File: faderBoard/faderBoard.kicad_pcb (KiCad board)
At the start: 2 copper layers, 80 x 80 mm, 22 parts, among them J1 Conn_01x14_Pin, J2 Conn_01x14_Socket, U1 ADS1115IDGS

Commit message: placed pinHeaders
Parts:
- J1, J2: moved to B.Cu
- moved J2 123.3 mm to (69.8, 23.4), turned to 180 degrees
- moved J1 65.5 mm to (4.00, 23.5), turned to 180 degrees
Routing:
- net in2: track 0.00 -> 70.0 mm
- net in1: track 0.00 -> 70.0 mm
- net Net-(J1-Pin_9): track 0.00 -> 70.0 mm
- net Net-(J1-Pin_14): track 0.00 -> 70.0 mm
- net Net-(J1-Pin_13): track 0.00 -> 70.0 mm
- net Net-(J1-Pin_12): track 0.00 -> 70.0 mm
- net Net-(J1-Pin_11): track 0.00 -> 70.0 mm
- net Net-(J1-Pin_10): track 0.00 -> 70.0 mm

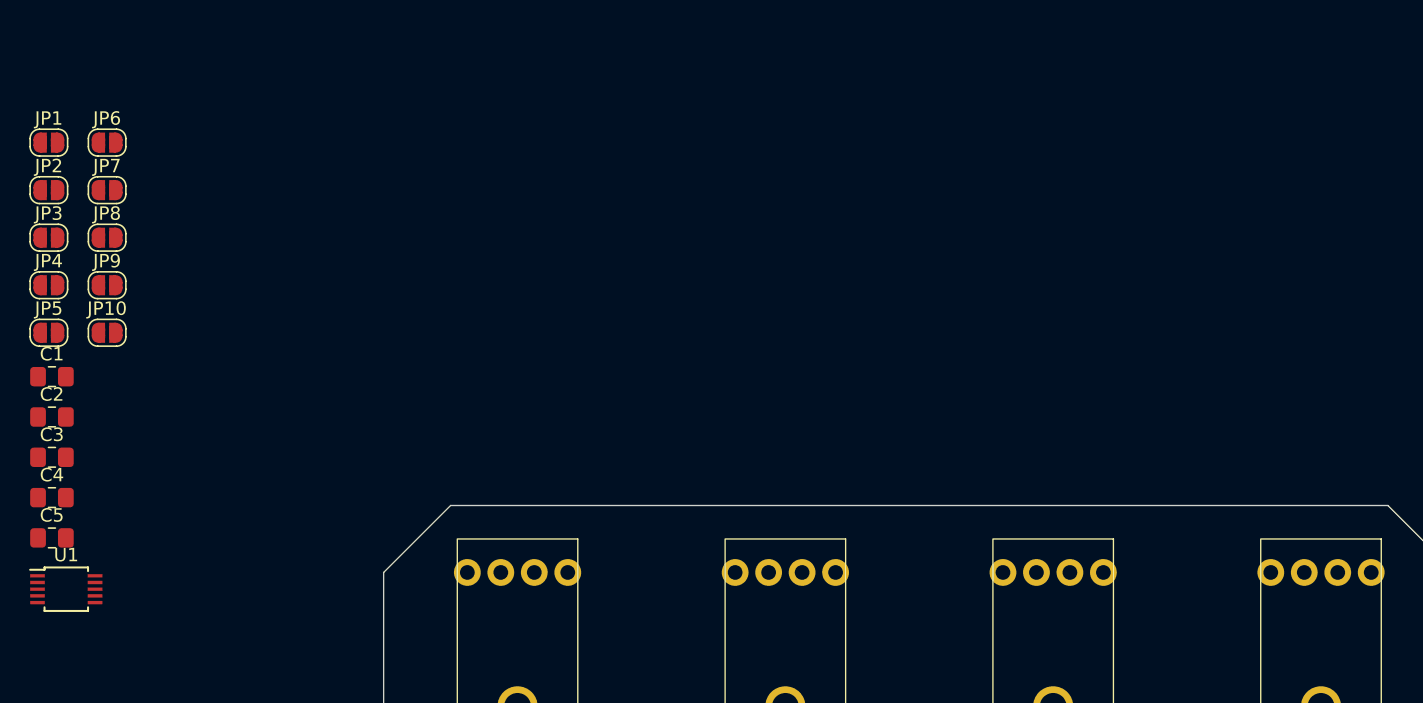
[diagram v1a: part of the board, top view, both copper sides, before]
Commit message: placed fader caps
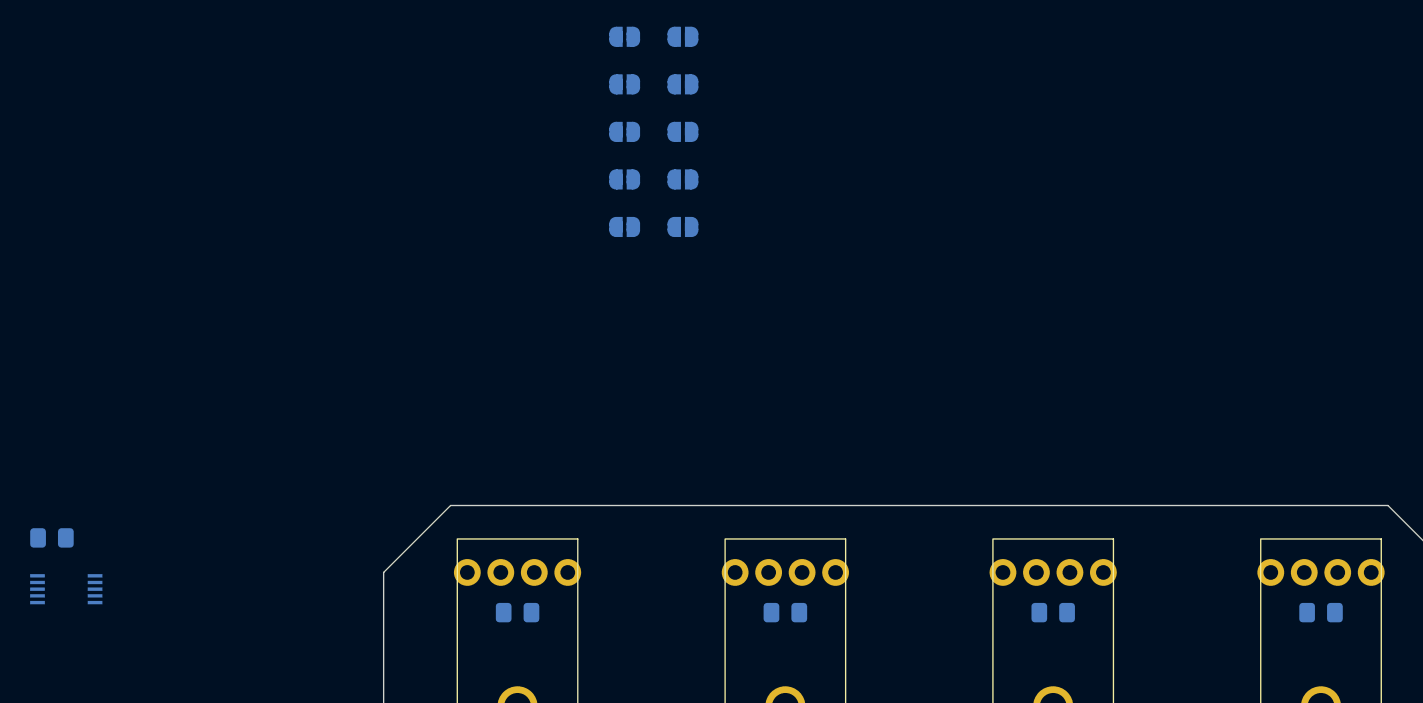
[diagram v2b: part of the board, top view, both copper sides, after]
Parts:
- C1, C2, C3, C4, C5, JP1, JP10, JP2, JP3, JP4, JP5, JP6, JP7, JP8, JP9, U1: moved to B.Cu
- moved C4 95.2 mm to (70.0, 8.00)
- moved C3 75.7 mm to (50.0, 8.00)
- moved C2 56.7 mm to (30.0, 8.00)
- moved JP1 43.7 mm to (18.0, -35.0), turned to 180 degrees
- moved JP10 43.7 mm to (22.4, -20.8), turned to 180 degrees
- moved JP2 43.7 mm to (18.0, -31.4), turned to 180 degrees
- moved JP3 43.7 mm to (18.0, -27.9), turned to 180 degrees
- moved JP4 43.7 mm to (18.0, -24.4), turned to 180 degrees
- moved JP5 43.7 mm to (18.0, -20.8), turned to 180 degrees
- moved JP6 43.7 mm to (22.4, -35.0), turned to 180 degrees
- moved JP7 43.7 mm to (22.4, -31.4), turned to 180 degrees
- moved JP8 43.7 mm to (22.4, -27.9), turned to 180 degrees
- moved JP9 43.7 mm to (22.4, -24.4), turned to 180 degrees
- moved C1 39.0 mm to (10.0, 8.00), turned to 180 degrees
- turned C5 to 180 degrees
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
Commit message: placed adc
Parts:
- moved C5 65.4 mm to (40.0, 12.0)
- moved U1 64.3 mm to (40.0, 15.0), turned to 0 degrees
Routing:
- net Fader4: track 0.00 -> 35.7 mm
- net Fader1: track 0.00 -> 28.0 mm
- net Fader3: track 0.00 -> 15.5 mm
- net Fader2: track 0.00 -> 13.4 mm
- net VCC: track 0.00 -> 3.96 mm
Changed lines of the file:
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@@
   )
   (footprint "Package_SO:TSSOP-10_3x3mm_P0.5mm" (layer "B.Cu")
-    (at -23.7 6.25 180)
+    (at 40 15)
     (descr "TSSOP10: plastic thin shrink small outline package; 10 leads; body width 3 mm; (see NXP SSOP-TSSOP-VSO-REFLOW.pdf and sot552-1_po.pdf)")
     (tags "SSOP 0.5")
@@
     (fp_line (start 1.5 1.5) (end 1.5 -1.5)
       (stroke (width 0.1) (type solid)) (layer "B.Fab"))
-    (pad "1" smd rect (at -2.15 1 180) (size 1.1 0.25) (layers "B.Cu" "B.Paste" "B.Mask")
+    (pad "1" smd rect (at -2.15 1) (size 1.1 0.25) (layers "B.Cu" "B.Paste" "B.Mask")
       (net 22 "ADDR") (pinfunction "ADDR") (pintype "input"))
-    (pad "2" smd rect (at -2.15 0.5 180) (size 1.1 0.25) (layers "B.Cu" "B.Paste" "B.Mask")
+    (pad "2" smd rect (at -2.15 0.5) (size 1.1 0.25) (layers "B.Cu" "B.Paste" "B.Mask")
       (net 35 "ALERT") (pinfunction "ALERT/RDY") (pintype "output"))
-    (pad "3" smd rect (at -2.15 0 180) (size 1.1 0.25) (layers "B.Cu" "B.Paste" "B.Mask")
+    (pad "3" smd rect (at -2.15 0) (size 1.1 0.25) (layers "B.Cu" "B.Paste" "B.Mask")
       (net 1 "GND") (pinfunction "GND") (pintype "power_in"))
-    (pad "4" smd rect (at -2.15 -0.5 180) (size 1.1 0.25) (layers "B.Cu" "B.Paste" "B.Mask")
+    (pad "4" smd rect (at -2.15 -0.5) (size 1.1 0.25) (layers "B.Cu" "B.Paste" "B.Mask")
       (net 2 "Fader1") (pinfunction "AIN0") (pintype "input"))
-    (pad "5" smd rect (at -2.15 -1 180) (size 1.1 0.25) (layers "B.Cu" "B.Paste" "B.Mask")
+    (pad "5" smd rect (at -2.15 -1) (size 1.1 0.25) (layers "B.Cu" "B.Paste" "B.Mask")
       (net 3 "Fader2") (pinfunction "AIN1") (pintype "input"))
-    (pad "6" smd rect (at 2.15 -1 180) (size 1.1 0.25) (layers "B.Cu" "B.Paste" "B.Mask")
+    (pad "6" smd rect (at 2.15 -1) (size 1.1 0.25) (layers "B.Cu" "B.Paste" "B.Mask")
       (net 4 "Fader3") (pinfunction "AIN2") (pintype "input"))
-    (pad "7" smd rect (at 2.15 -0.5 180) (size 1.1 0.25) (layers "B.Cu" "B.Paste" "B.Mask")
+    (pad "7" smd rect (at 2.15 -0.5) (size 1.1 0.25) (layers "B.Cu" "B.Paste" "B.Mask")
       (net 5 "Fader4") (pinfunction "AIN3") (pintype "input"))
-    (pad "8" smd rect (at 2.15 0 180) (size 1.1 0.25) (layers "B.Cu" "B.Paste" "B.Mask")
+    (pad "8" smd rect (at 2.15 0) (size 1.1 0.25) (layers "B.Cu" "B.Paste" "B.Mask")
       (net 6 "VCC") (pinfunction "VDD") (pintype "power_in"))
-    (pad "9" smd rect (at 2.15 0.5 180) (size 1.1 0.25) (layers "B.Cu" "B.Paste" "B.Mask")
+    (pad "9" smd rect (at 2.15 0.5) (size 1.1 0.25) (layers "B.Cu" "B.Paste" "B.Mask")
       (net 7 "SDA") (pinfunction "SDA") (pintype "bidirectional"))
-    (pad "10" smd rect (at 2.15 1 180) (size 1.1 0.25) (layers "B.Cu" "B.Paste" "B.Mask")
+    (pad "10" smd rect (at 2.15 1) (size 1.1 0.25) (layers "B.Cu" "B.Paste" "B.Mask")
       (net 8 "SCL") (pinfunction "SCL") (pintype "input"))
     (model "${KICAD6_3DMODEL_DIR}/Package_SO.3dshapes/TSSOP-10_3x3mm_P0.5mm.wrl"
@@
   )
   (footprint "Capacitor_SMD:C_0805_2012Metric_Pad1.18x1.45mm_HandSolder" (layer "B.Cu")
-    (at -24.77 2.42 180)
+    (at 39.9625 12 180)
     (descr "Capacitor SMD 0805 (2012 Metric), square (rectangular) end terminal, IPC_7351 nominal with elongated pad for handsoldering. (Body size source: IPC-SM-782 page 76, https://www.pcb-3d.com/wordpress/wp-content/uploads/ipc-sm-782a_amendment_1_and_2.pdf, https://docs.google.com/spreadsheets/d/1BsfQQcO9C6DZCsRaXUlFlo91Tg2WpOkGARC1WS5S8t0/edit?usp=sharing), generated with kicad-footprint-generator")
     (tags "capacitor handsolder")
@@
     )
     (stroke (width 0.1) (type solid)) (fill none) (layer "Edge.Cuts"))
+  (segment (start 37.85 14.5) (end 32.08094 14.5) (width 0.25) (layer "B.Cu") (net 2))
+  (segment (start 32.08094 14.5) (end 22.58094 5) (width 0.25) (layer "B.Cu") (net 2))
+  (segment (start 22.58094 5) (end 13.75 5) (width 0.25) (layer "B.Cu") (net 2))
+  (segment (start 31.0375 8) (end 31.0375 7.7125) (width 0.25) (layer "B.Cu") (net 3))
+  (segment (start 31.0375 7.7125) (end 33.75 5) (width 0.25) (layer "B.Cu") (net 3))
+  (segment (start 37.85 14) (end 37.0375 14) (width 0.25) (layer "B.Cu") (net 3))
+  (segment (start 37.0375 14) (end 31.0375 8) (width 0.25) (layer "B.Cu") (net 3))
+  (segment (start 51.0375 7.7125) (end 53.75 5) (width 0.25) (layer "B.Cu") (net 4))
+  (segment (start 42.15 14) (end 45.0375 14) (width 0.25) (layer "B.Cu") (net 4))
+  (segment (start 45.0375 14) (end 51.0375 8) (width 0.25) (layer "B.Cu") (net 4))
+  (segment (start 51.0375 8) (end 51.0375 7.7125) (width 0.25) (layer "B.Cu") (net 4))
+  (segment (start 53.36906 9.05) (end 69.9875 9.05) (width 0.25) (layer "B.Cu") (net 5))
+  (segment (start 42.15 14.5) (end 47.91906 14.5) (width 0.25) (layer "B.Cu") (net 5))
+  (segment (start 71.0375 7.7125) (end 73.75 5) (width 0.25) (layer "B.Cu") (net 5))
+  (segment (start 71.0375 8) (end 71.0375 7.7125) (width 0.25) (layer "B.Cu") (net 5))
+  (segment (start 47.91906 14.5) (end 53.36906 9.05) (width 0.25) (layer "B.Cu") (net 5))
+  (segment (start 69.9875 9.05) (end 71.0375 8) (width 0.25) (layer "B.Cu") (net 5))
+  (segment (start 42.15 15) (end 41.325 15) (width 0.25) (layer "B.Cu") (net 6))
+  (segment (start 41.325 15) (end 41 14.675) (width 0.25) (layer "B.Cu") (net 6))
+  (segment (start 41 14.675) (end 41 12) (width 0.25) (layer "B.Cu") (net 6))
   (segment (start 59.59 38.74) (end 69.8 28.53) (width 0.5) (layer "F.Cu") (net 10))
   (segment (start 4 38.74) (end 59.59 38.74) (width 0.5) (layer "F.Cu") (net 10))

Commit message: routing
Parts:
- moved JP6 65.2 mm to (27.0, 30.0), turned to 0 degrees
- moved JP1 62.1 mm to (14.0, 27.0), turned to 0 degrees
- moved JP2 61.6 mm to (14.0, 30.0), turned to 0 degrees
- moved JP7 61.1 mm to (40.0, 27.0)
- moved JP3 61.0 mm to (14.0, 33.0), turned to 0 degrees
- moved JP8 60.5 mm to (40.0, 30.0)
- moved JP4 60.5 mm to (14.0, 36.0), turned to 0 degrees
- moved JP9 60.0 mm to (40.0, 33.0)
- moved JP10 59.5 mm to (40.0, 36.0)
- moved JP5 48.6 mm to (27.0, 27.0), turned to 0 degrees
- turned C1 to 0 degrees
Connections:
- J1 pad 6: out3 -> out4
- JP4 pad 1: out3 -> out4
- JP6 pad 2: in1 -> in2
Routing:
- net VCC: track 3.96 -> 77.7 mm
- net Fader4: track 35.7 -> 107.6 mm, vias 0 -> 1
- net SDA: track 0.00 -> 67.4 mm
- net SCL: track 0.00 -> 63.1 mm
- net Fader3: track 15.5 -> 77.2 mm, vias 0 -> 1
- net Fader2: track 13.4 -> 48.9 mm, vias 0 -> 1
- net Fader1: track 28.0 -> 60.7 mm, vias 0 -> 1
- net ADDR: track 0.00 -> 22.8 mm, vias 0 -> 2
- net in1: track 70.0 -> 83.2 mm, vias 0 -> 3
- net in2: track 70.0 -> 82.2 mm, vias 0 -> 3
- net out3: track 0.00 -> 9.62 mm
- net out4: track 0.00 -> 9.43 mm
- net GND: track 0.00 -> 4.07 mm, vias 0 -> 9
- added copper zone on B.Cu, net GND
- added copper zone on F.Cu, net GND
- added copper zone on F.Cu, net VCC

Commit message: labels and fixes
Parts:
- added ?: , MountingHole:MountingHole_3.2mm_M3, F.Cu at (60.0, 5.00)
- added ?: , MountingHole:MountingHole_3.2mm_M3, F.Cu at (20.0, 75.0)
- added ?: , MountingHole:MountingHole_3.2mm_M3, F.Cu at (60.0, 75.0)
- added ?: , MountingHole:MountingHole_3.2mm_M3, F.Cu at (20.0, 5.00)
- moved JP1 4.35 mm to (18.4, 27.0)
- moved JP2 4.35 mm to (18.4, 30.0)
- moved JP3 4.35 mm to (18.4, 33.0)
- moved JP4 4.35 mm to (18.4, 36.0)
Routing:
- net Fader4: track 107.6 -> 103.3 mm
- net out4: track 9.43 -> 13.8 mm
- net out3: track 9.62 -> 14.0 mm
- net Fader3: track 77.2 -> 72.8 mm
- net Fader2: track 48.9 -> 46.9 mm
- net Fader1: track 60.7 -> 62.0 mm
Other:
- board text added: "00 01 10 11"
- board text added: "Address"
- board text added: "Fader"
- board text added: "VCC GND F1 F2 F3 F4 F5 F6 F7 F8 F9 F10 F11 F12"
- board text added: "VCC GND SDA/F1 SCL/F2 F3 F4 F5 F6 F7 F8 F9 F10 F11 F12"
- board text added: "i2c"

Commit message: connected Alert pin
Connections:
- J1 pad 5: out3 -> ALERT
- JP3 pad 1: out3 -> ALERT
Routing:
- net ALERT: track 0.00 -> 56.3 mm, vias 0 -> 1
- net out3: track 14.0 -> 0.00 mm
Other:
- board text added: "VCC GND SDA/F1 SCL/F2 Alert/F3 F4 F5 F6 Alert2/F7 F8 F9 F10 F11 Alert3/F12"

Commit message: fader board small changes
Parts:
- added J1: Conn_01x14_Pin, Connector_PinHeader_2.54mm:PinHeader_1x14_P2.54mm_Vertical, B.Cu at (3.50, 23.4)
- added J2: Conn_01x14_Socket, Connector_PinSocket_2.54mm:PinSocket_1x14_P2.54mm_Vertical, B.Cu at (76.5, 23.4)
- J1: footprint Connector_PinHeader_2.54mm:PinHeader_1x14_P2.54mm_Horizontal -> Connector_PinHeader_2.54mm:PinHeader_1x14_P2.54mm_Vertical
- J2: footprint Connector_PinSocket_2.54mm:PinSocket_1x14_P2.54mm_Horizontal -> Connector_PinSocket_2.54mm:PinSocket_1x14_P2.54mm_Vertical
- moved J2 9.95 mm to (79.8, 23.4)
- moved J1 3.75 mm to (0.25, 23.4)
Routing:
- net in1: track 83.2 -> 97.0 mm, vias 3 -> 1
- net Net-(J1-Pin_9): track 70.0 -> 82.7 mm
- net Net-(J1-Pin_14): track 70.0 -> 82.7 mm
- net Net-(J1-Pin_13): track 70.0 -> 82.7 mm
- net Net-(J1-Pin_12): track 70.0 -> 82.7 mm
- net Net-(J1-Pin_11): track 70.0 -> 82.7 mm
- net Net-(J1-Pin_10): track 70.0 -> 82.7 mm
- net in2: track 82.2 -> 94.4 mm, vias 3 -> 1
- net Fader1: track 62.0 -> 50.0 mm, vias 1 -> 0
- net VCC: track 77.7 -> 82.3 mm
- net SDA: track 67.4 -> 70.4 mm
- net unconnected-(J2-Pin_14-Pad14): track 0.00 -> 3.00 mm
- net unconnected-(J2-Pin_13-Pad13): track 0.00 -> 3.00 mm
- net unconnected-(J2-Pin_12-Pad12): track 0.00 -> 3.00 mm
- net unconnected-(J2-Pin_11-Pad11): track 0.00 -> 3.00 mm
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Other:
- board text added: "JLCJLCJLCJLC"

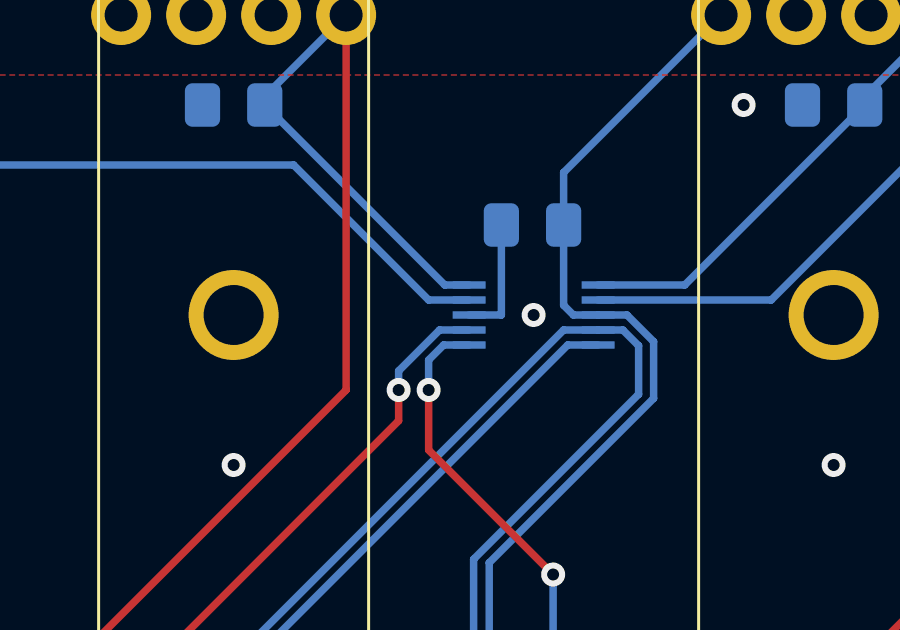
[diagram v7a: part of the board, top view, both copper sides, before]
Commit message: fader board changes
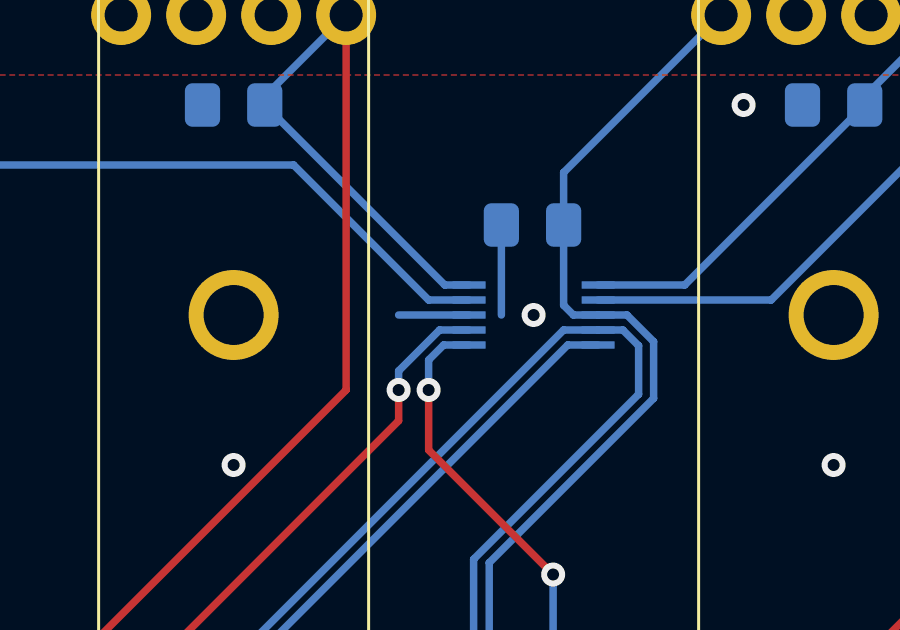
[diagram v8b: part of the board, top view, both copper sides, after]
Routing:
- net GND: track 4.07 -> 5.35 mm
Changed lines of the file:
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@@
   (via (at 47 8) (size 0.8) (drill 0.4) (layers "F.Cu" "B.Cu") (free) (net 1))
   (segment (start 38.925 15) (end 38.925 12) (width 0.25) (layer "B.Cu") (net 1))
-  (segment (start 37.85 15) (end 38.925 15) (width 0.25) (layer "B.Cu") (net 1))
+  (segment (start 37.85 15) (end 35.5 15) (width 0.25) (layer "B.Cu") (net 1))
   (segment (start 36.5 14.5) (end 32 10) (width 0.25) (layer "B.Cu") (net 2))
   (segment (start 11.0375 7.7125) (end 11.0375 8) (width 0.25) (layer "B.Cu") (net 2))
